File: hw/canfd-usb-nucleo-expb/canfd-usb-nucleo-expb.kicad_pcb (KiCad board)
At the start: 2 copper layers, 70 x 59 mm, 58 parts, among them CN1 POWER, CN2 CONN, J1 USB_C_Receptacle_USB2.0, J2 Conn_01x10, J3 Conn_01x10, J4 Conn_01x10, SW1 SW_Push_Dual_x2, SW2 SW_Push_Dual_x2, SW3 SW_Push_Dual_x2, U1 USBLC6-2SC6, U2 ATA6561-GAQW-N, U3 ATA6561-GAQW-N, U4 ATA6561-GAQW-N

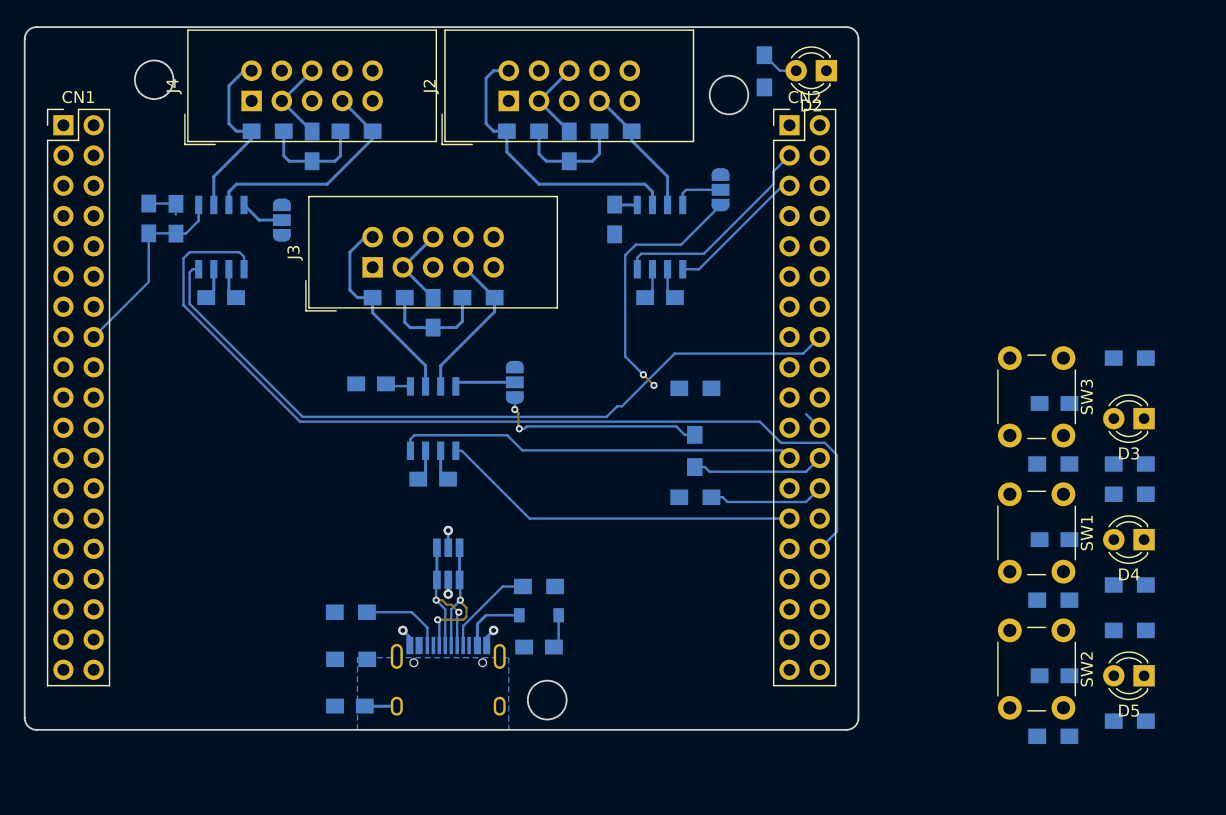
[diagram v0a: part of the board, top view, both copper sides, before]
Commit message: HW: PCB routing branched-off by AlexeyZ
Seems like I've started some work in parallel with Stiwens
so this is my version of the PCB routing from the last commit.
Probably this branch will be deleted and not used in the final
design but that's just a little bit of practice on my side.

Signed-off-by: AlexeyZ <silkt207@gmail.com>
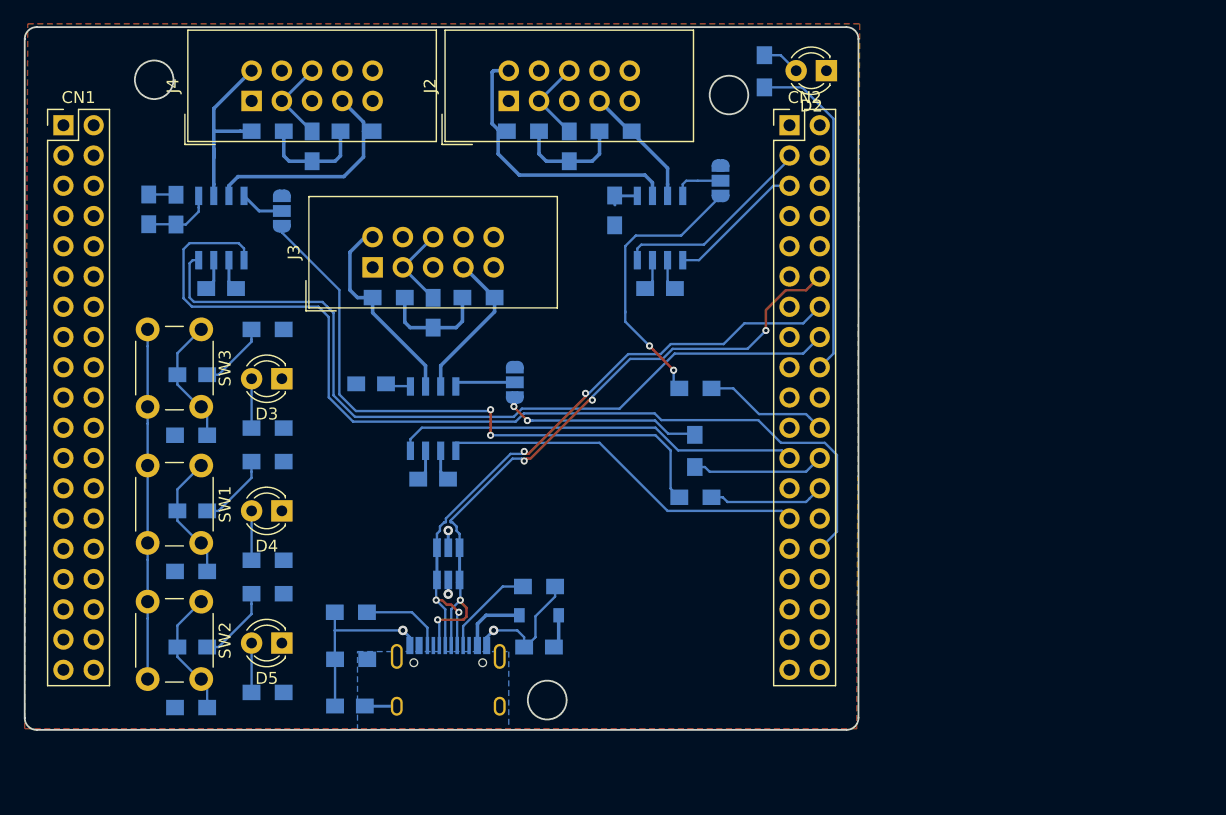
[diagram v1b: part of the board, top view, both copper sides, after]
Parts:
- moved R8 73.8 mm to (122.6, 106.3), turned to 180 degrees
- moved R14 72.9 mm to (122.6, 117.4), turned to 180 degrees
- moved D3 72.5 mm to (123.8, 99.4)
- moved R11 72.5 mm to (122.6, 103.5)
- moved D5 72.4 mm to (123.8, 121.6)
- moved D4 72.4 mm to (123.8, 110.5)
- moved R15 72.4 mm to (116.2, 104.1)
- moved R7 72.4 mm to (116.2, 115.6)
- moved R9 72.4 mm to (116.2, 127.0)
- moved C4 72.4 mm to (116.3, 110.5)
- moved C5 72.4 mm to (116.3, 121.9)
- moved C6 72.4 mm to (116.3, 99.1)
- moved R13 72.4 mm to (122.6, 125.7)
- moved R16 72.4 mm to (122.6, 95.2), turned to 180 degrees
- moved SW1 72.4 mm to (117.1, 106.7)
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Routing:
- net STANDBY_3: track 0.00 -> 51.4 mm, vias 0 -> 2
- net D+: track 15.2 -> 59.5 mm, vias 2 -> 5
- net D-: track 14.0 -> 56.7 mm, vias 2 -> 4
- net LED1: track 0.00 -> 28.2 mm
- net GND: track 36.0 -> 59.4 mm
- net +3V3: track 20.4 -> 39.2 mm
- net SW3: track 0.00 -> 10.8 mm
- net SW2: track 0.00 -> 10.8 mm
- net SW1: track 0.00 -> 10.8 mm
- net Net-(CN2-Pad22): track 2.07 -> 10.9 mm
- net Net-(C5-Pad1): track 0.00 -> 6.57 mm
- net Net-(C4-Pad1): track 0.00 -> 6.24 mm
- net Net-(C6-Pad1): track 0.00 -> 5.91 mm
- net TX3: track 79.0 -> 83.9 mm
- net RX3: track 63.3 -> 67.8 mm
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- added copper zone on F.Cu, net GND

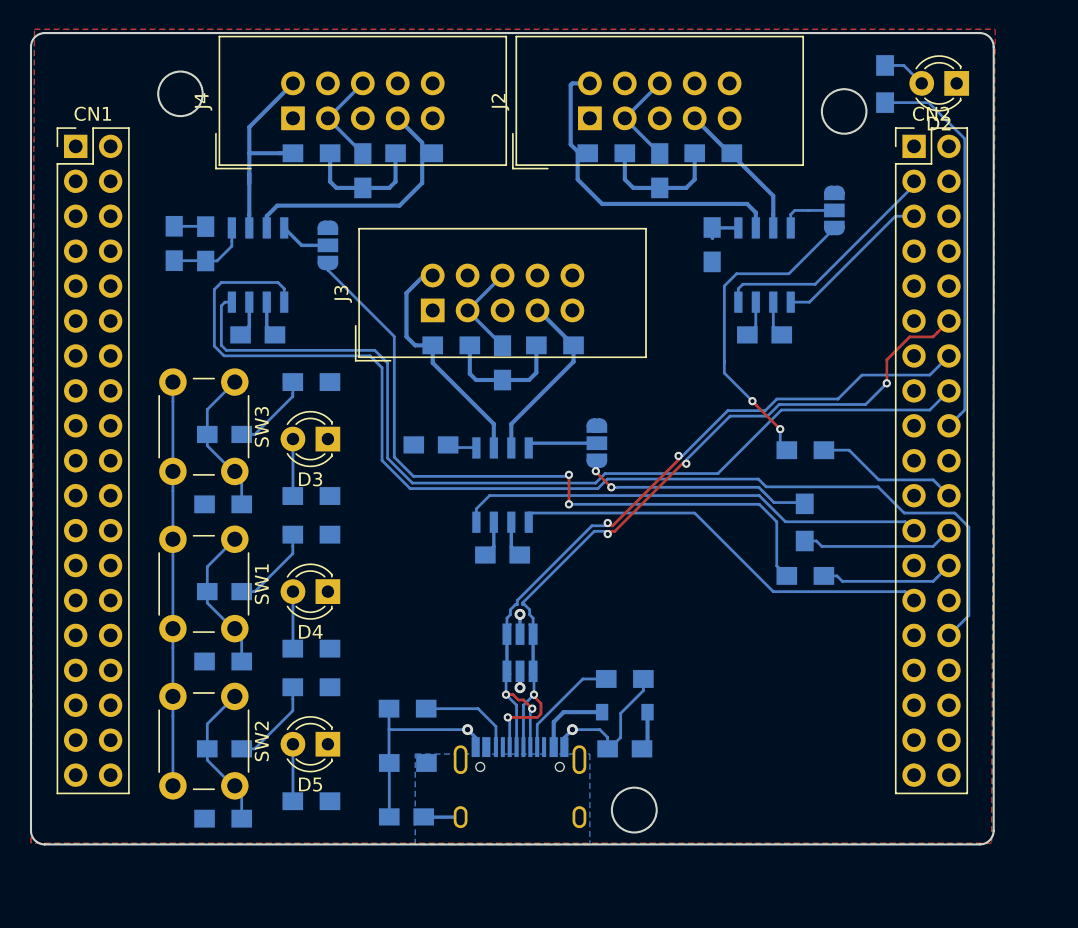
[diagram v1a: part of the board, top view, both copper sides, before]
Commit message: HW: First version of PCB layout
First version of PCB layout is ready for review.
Changed the assignments of pins for switches and status LEDs
to ease the routing of traces.
PCB's bottom layer is GND plane, most of the traces are placed
on top layer. Ground planes are connected with via stitching on
full area of the PCB.
There are no high speed signals on this PCB that might be of a concern
while routing so general rules of keeping the traces short and diff pairs
of the same lenghts are used.

Signed-off-by: AlexeyZ <silkt207@gmail.com>
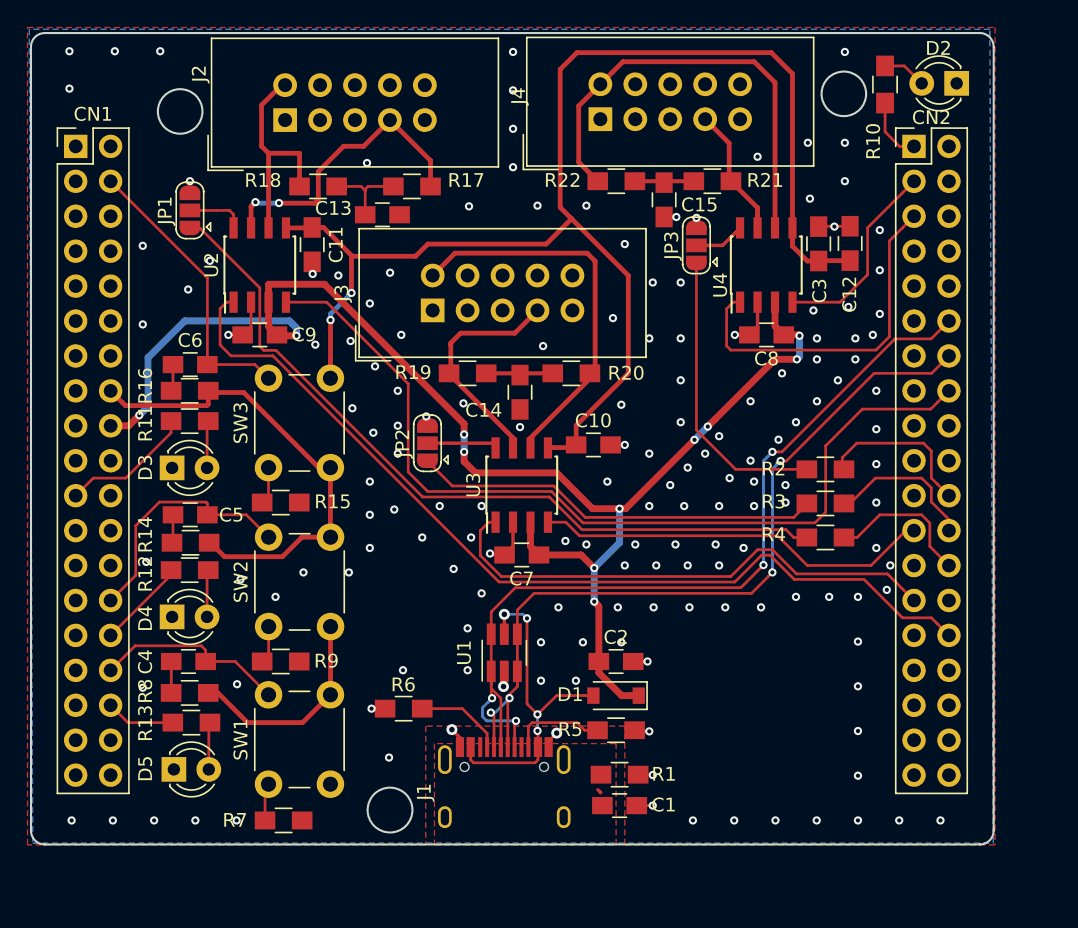
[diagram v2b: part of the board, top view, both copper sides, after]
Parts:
- C1, C10, C11, C12, C13, C14, C15, C2, C3, C4, C5, C6, C7, C8, C9, D1, J1, JP1, JP2, JP3, R1, R10, R11, R12, R13, R14, R15, R16, R17, R18, R19, R2, R20, R21, R22, R3, R4, R5, R6, R7, R8, R9, U1, U2, U3, U4: moved to F.Cu
- CN1: value POWER -> Conn_02x19_Odd_Even
- moved C12 49.1 mm to (161.8, 85.2)
- moved JP1 46.9 mm to (113.8, 82.8)
- moved C3 44.6 mm to (159.5, 85.2)
- moved C8 37.0 mm to (155.7, 91.8), turned to 180 degrees
- moved U4 37.0 mm to (155.7, 86.7)
- moved C9 36.7 mm to (118.9, 91.8), turned to 180 degrees
- moved U2 36.7 mm to (118.9, 86.7)
- moved C11 29.1 mm to (122.7, 85.3)
- moved JP3 26.8 mm to (150.6, 85.3)
- moved J4 22.4 mm to (143.6, 76.1)
- moved R22 22.3 mm to (144.8, 80.6)
- moved J2 22.2 mm to (120.7, 76.2)
- moved R17 22.0 mm to (129.9, 81.0)
- moved C15 22.0 mm to (148.3, 82.0), turned to 270 degrees
- moved R21 21.8 mm to (151.8, 80.6)
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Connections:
- CN1 pad 21: (no net) -> LED2
- CN1 pad 28: (no net) -> SW2
- CN1 pad 30: (no net) -> LED3
- CN1 pad 32: (no net) -> SW1
- CN1 pad 34: (no net) -> LED4
- CN1 pad 4: (no net) -> SW3
- CN2 pad 1: SW1 -> LED1
- CN2 pad 16: RX3 -> RX1
- CN2 pad 18: LED1 -> (no net)
- CN2 pad 19: LED3 -> (no net)
- CN2 pad 2: SW2 -> (no net)
- CN2 pad 21: LED2 -> (no net)
- CN2 pad 3: RX1 -> RX3
- CN2 pad 30: TX3 -> TX1
- CN2 pad 33: LED4 -> (no net)
- CN2 pad 4: SW3 -> (no net)
- CN2 pad 5: TX1 -> TX3
- R2 pad 2: STANDBY_1 -> STANDBY_3
- R4 pad 2: STANDBY_3 -> STANDBY_1
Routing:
- net +3V3: track 39.2 -> 150.8 mm, vias 0 -> 2
- net +5V: track 10.7 -> 105.6 mm, vias 0 -> 11
- net TX3: track 83.9 -> 25.7 mm
- net TX1: track 12.1 -> 67.2 mm
- net RX3: track 67.8 -> 14.5 mm
- net RX1: track 17.2 -> 65.4 mm
- net STANDBY_1: track 23.7 -> 56.7 mm, vias 2 -> 0
- net GND: track 59.4 -> 27.4 mm, vias 3 -> 157
- net STANDBY_3: track 51.4 -> 21.2 mm, vias 2 -> 0
- net LED1: track 28.2 -> 4.64 mm
- net Net-(D1-Pad2): track 7.08 -> 24.5 mm, vias 1 -> 4
- net CAN3_N: track 15.8 -> 32.9 mm
- net SW3: track 10.8 -> 23.8 mm
- net STANDBY_2: track 17.0 -> 29.4 mm, vias 2 -> 0
- net CAN2_N: track 17.1 -> 28.3 mm
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- added copper zone on B.Cu, net GND
- added copper zone on F.Cu, net Net-(C1-Pad1)
- removed copper zone on B.Cu, net Net-(C1-Pad1)
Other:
- outline, holes or cut-outs redrawn
